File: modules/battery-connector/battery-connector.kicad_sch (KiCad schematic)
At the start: 1 part, among them J1 691210910002

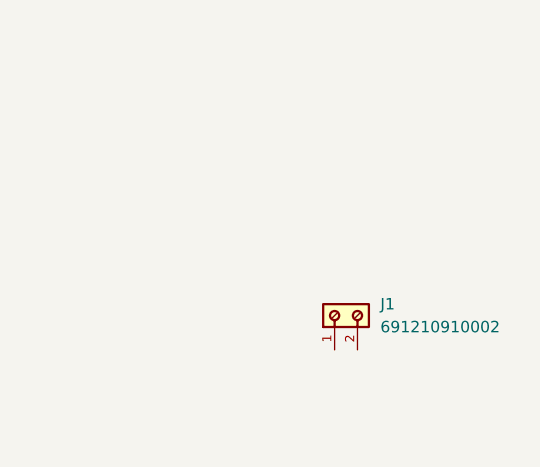
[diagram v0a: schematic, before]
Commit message: finish battery connector module design
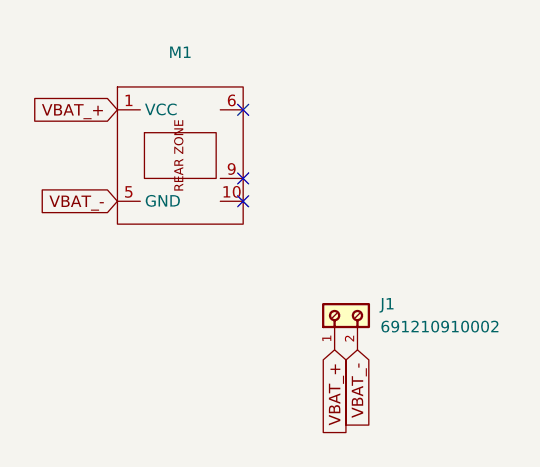
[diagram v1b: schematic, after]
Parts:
- added M1: ~, MegaCastle:MegaCastle2x5-Module-I7.0x7.9-M8CC-PANEL-NIBBLE, symbol MegaCastle:MegaCastle2x5-Module-I7.0x7.9-M8CC
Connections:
- net VBAT_+: now reaches J1.1
- net VBAT_+: now also M1.1 (VCC)
- net VBAT_-: now reaches J1.2
- net VBAT_-: now also M1.5 (GND)
- no-connect marks 0 -> 3
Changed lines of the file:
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@@
 	(generator_version "8.0")
 	(paper "A4")
+	(no_connect
+		(at 113.03 41.91)
+	)
+	(no_connect
+		(at 113.03 34.29)
+	)
+	(no_connect
+		(at 113.03 44.45)
+	)
+	(global_label "VBAT_+"
+		(shape input)
+		(at 99.06 34.29 180)
+		(fields_autoplaced yes)
+		(effects
+			(font
+				(size 1.27 1.27)
+			)
+			(justify right)
+		)
+		(property "Intersheetrefs" "${INTERSHEET_REFS}"
+			(at 89.12 34.29 0)
+			(effects
+				(font
+					(size 1.27 1.27)
+				)
+				(justify right)
+				(hide yes)
+			)
+		)
+	)
+	(global_label "VBAT_-"
+		(shape input)
+		(at 99.06 44.45 180)
+		(fields_autoplaced yes)
+		(effects
+			(font
+				(size 1.27 1.27)
+			)
+			(justify right)
+		)
+		(property "Intersheetrefs" "${INTERSHEET_REFS}"
+			(at 89.12 44.45 0)
+			(effects
+				(font
+					(size 1.27 1.27)
+				)
+				(justify right)
+				(hide yes)
+			)
+		)
+	)
+	(global_label "VBAT_-"
+		(shape input)
+		(at 125.73 60.96 270)
+		(fields_autoplaced yes)
+		(effects
+			(font
+				(size 1.27 1.27)
+			)
+			(justify right)
+		)
+		(property "Intersheetrefs" "${INTERSHEET_REFS}"
+			(at 125.73 70.9 90)
+			(effects
+				(font
+					(size 1.27 1.27)
+				)
+				(justify right)
+				(hide yes)
+			)
+		)
+	)
+	(global_label "VBAT_+"
+		(shape input)
+		(at 123.19 60.96 270)
+		(fields_autoplaced yes)
+		(effects
+			(font
+				(size 1.27 1.27)
+			)
+			(justify right)
+		)
+		(property "Intersheetrefs" "${INTERSHEET_REFS}"
+			(at 123.19 70.9 90)
+			(effects
+				(font
+					(size 1.27 1.27)
+				)
+				(justify right)
+				(hide yes)
+			)
+		)
+	)
+	(symbol
+		(lib_id "MegaCastle:MegaCastle2x5-Module-I7.0x7.9-M8CC")
+		(at 105.41 39.37 0)
+		(unit 1)
+		(exclude_from_sim no)
+		(in_bom yes)
+		(on_board yes)
+		(dnp no)
+		(fields_autoplaced yes)
+		(property "Reference" "M1"
+			(at 106.045 27.94 0)
+			(effects
+				(font
+					(size 1.27 1.27)
+				)
+			)
+		)
+		(property "Value" "~"
+			(at 106.045 30.48 0)
+			(effects
+				(font
+					(size 1.27 1.27)
+				)
+			)
+		)
+		(property "Footprint" "MegaCastle:MegaCastle2x5-Module-I7.0x7.9-M8CC-PANEL-NIBBLE"
+			(at 105.41 52.07 0)
+			(effects
+				(font
+					(size 1.27 1.27)
+				)
+				(hide yes)
+			)
+		)
+		(property "Datasheet" ""
+			(at 105.41 34.29 0)
+			(effects
+				(font
+					(size 1.27 1.27)
+				)
+				(hide yes)
+			)
+		)
+		(property "Description" "Generated using footprint-gen .. 7 8 5 M8CC"
+			(at 105.41 39.37 0)
+			(effects
+				(font
+					(size 1.27 1.27)
+				)
+				(hide yes)
+			)
+		)
+		(pin "5"
+		)
+		(pin "1"
+		)
+		(pin "6"
+		)
+		(pin "9"
+		)
+		(pin "10"
+		)
+		(instances
+			(project ""
+				(path "/de625f4d-017d-4e61-aaaf-647862dae6d9"
+					(reference "M1")
+					(unit 1)
+				)
+			)
+		)
+	)
 	(symbol
 		(lib_id "691210910002:691210910002")

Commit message: KiCad v9 adding new footprints
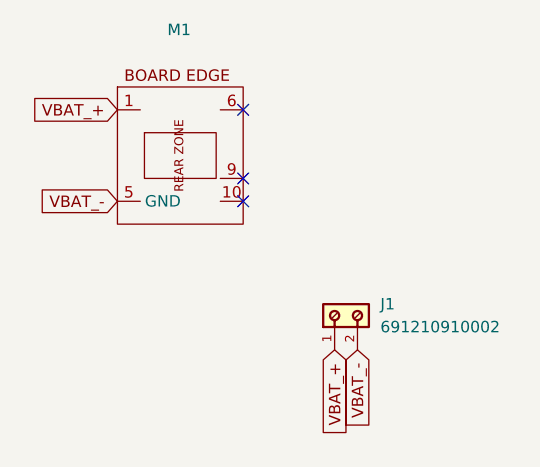
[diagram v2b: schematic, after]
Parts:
- J1: footprint footprints:691210910002 -> MegaCastle:691210910002
- M1: footprint MegaCastle:MegaCastle2x5-Module-I7.0x7.9-M8CC-PANEL-NIBBLE -> MegaCastle:MegaCastle2x5-Module-I15.0x7.9-M8CC-SPAREPAD; symbol MegaCastle:MegaCastle2x5-Module-I7.0x7.9-M8CC -> MegaCastle:MegaCastle2x5-Module-I7.0x7.9-M8CC-EDGE
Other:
- moved on the sheet: M1
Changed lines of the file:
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@@
 (kicad_sch
-	(version 20231120)
+	(version 20250114)
 	(generator "eeschema")
-	(generator_version "8.0")
+	(generator_version "9.0")
 	(paper "A4")
 	(no_connect
@@
 	)
 	(symbol
-		(lib_id "MegaCastle:MegaCastle2x5-Module-I7.0x7.9-M8CC")
+		(lib_id "MegaCastle:MegaCastle2x5-Module-I7.0x7.9-M8CC-EDGE")
 		(at 105.41 39.37 0)
 		(unit 1)
@@
 		(fields_autoplaced yes)
 		(property "Reference" "M1"
-			(at 106.045 27.94 0)
+			(at 105.9138 25.4 0)
 			(effects
 				(font
@@
 		)
 		(property "Value" "~"
-			(at 106.045 30.48 0)
-			(effects
-				(font
-					(size 1.27 1.27)
-				)
-			)
-		)
-		(property "Footprint" "MegaCastle:MegaCastle2x5-Module-I7.0x7.9-M8CC-PANEL-NIBBLE"
+			(at 105.9138 27.94 0)
+			(effects
+				(font
+					(size 1.27 1.27)
+				)
+			)
+		)
+		(property "Footprint" "MegaCastle:MegaCastle2x5-Module-I15.0x7.9-M8CC-SPAREPAD"
 			(at 105.41 52.07 0)
 			(effects
@@
 			)
 		)
-		(property "Footprint" "footprints:691210910002"
+		(property "Footprint" "MegaCastle:691210910002"
 			(at 125.73 55.88 0)
 			(effects
@@
 		)
 	)
+	(embedded_fonts no)
 )
